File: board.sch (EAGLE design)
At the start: 26 parts, among them J2 632723300011, Q1 16Mhz, U1 MICROCHIP_TECHNOLOGY_MIC5219-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

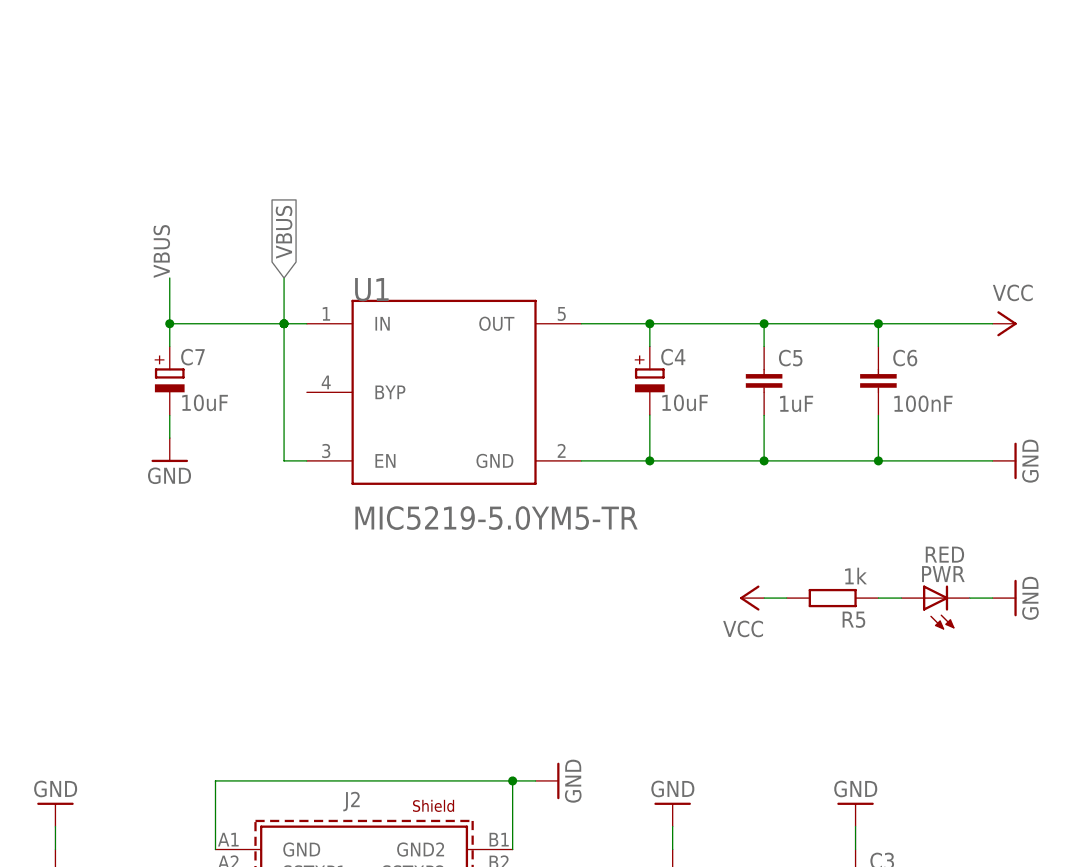
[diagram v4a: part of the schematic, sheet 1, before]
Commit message: Finish header; Add RX/TX LEDs
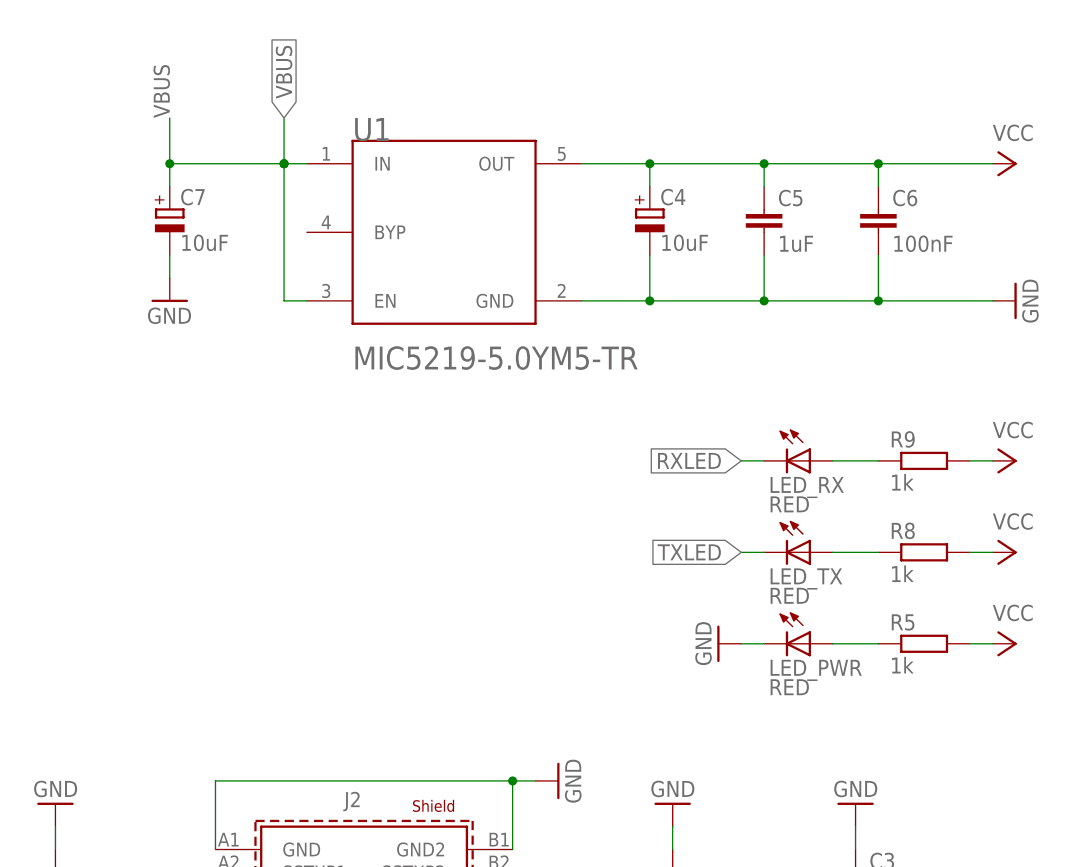
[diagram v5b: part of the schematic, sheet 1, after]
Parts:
- removed PWR: RED, adafruit:LEDCHIP-LED0805
- added JP_IO: (no value), pinhead:PINHD-1X6
- added JP_MISC: (no value), pinhead:PINHD-1X4
- added LED_PWR, LED_RX, LED_TX: RED, adafruit:LEDCHIP-LED0805
- added R7: 10k, rcl:R-EU_R0805
- added R8, R9: 1k, rcl:R-EU_R0805
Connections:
- new net IO10: JP_IO.3, U$1.PB6(OC1B/OC4B/ADC13)
- new net IO11: JP_IO.4, U$1.PB7(OC0A/OC1C/RTS)
- new net IO12: JP_IO.5, U$1.PD6(T1/ADC9/!OC4D)
- new net IO13: JP_IO.6, U$1.PC7(ICP3/CLK0/OC4A)
- new net IO8: JP_IO.1, U$1.PB4(ADC11)
- new net IO9: JP_IO.2, U$1.PB5(OC1A/ADC12/!OC4B)
- new net N$10: R7.1, U$1.PE2(!HWB)
- new net N$11: LED_TX.A, R8.1
- new net N$12: LED_RX.A, R9.1
- new net RXLED: LED_RX.C, U$1.PB0(SS)
- new net TXLED: LED_TX.C, U$1.PD5(XCK/CTS)
- net GND: now also JP_MISC.3, JP_MISC.4, LED_PWR.C, R7.2; no longer PWR.C
- net N$4: now also LED_PWR.A; no longer PWR.A
- net VCC: now also JP_MISC.1, JP_MISC.2, R8.2, R9.2
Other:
- moved on the sheet: C4, C5, C6, C7, R5, U1

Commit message: Add frames to sheets
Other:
- note added: "LEVY EHRSTEIN"
- note added: "SL-MICRO"
- moved on the sheet: C1, C10, C2, C3, C4, C5, C6, C7, C8, C9, ISP1, J2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
